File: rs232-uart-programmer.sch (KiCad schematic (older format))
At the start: 45 parts, among them J1 DB9_Female_MountingHoles, J2 Barrel_Jack, J3 Conn_01x03_Male, J4 Conn_01x02_Male, J5 USB_B, J6 Conn_01x05_Male, Q1 2N3905, Q2 AO3407A, Q3 2N3905, U1 L7805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

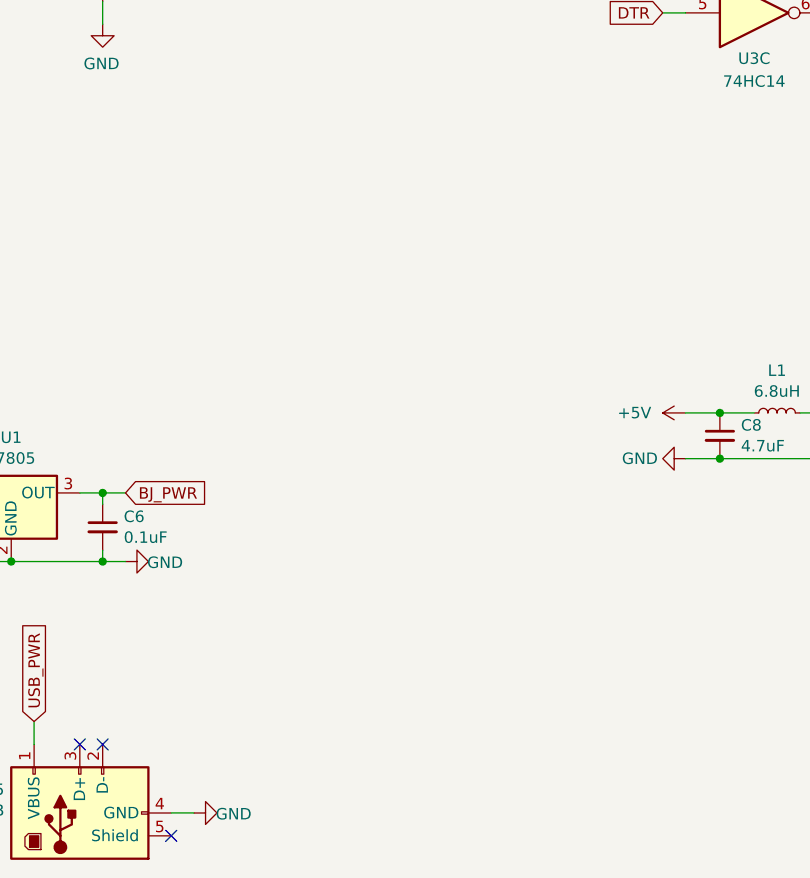
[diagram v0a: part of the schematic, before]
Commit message: Added mounting holes
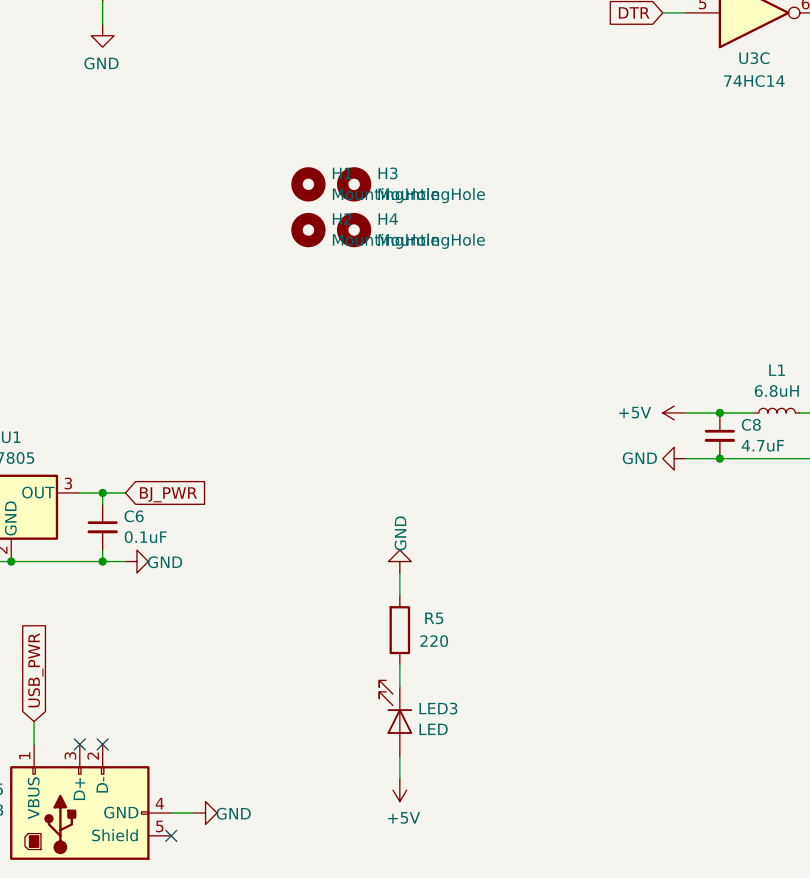
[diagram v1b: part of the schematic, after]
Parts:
- added H1, H2, H3, H4: MountingHole, MountingHole:MountingHole_3mm, symbol Mechanical:MountingHole
- added LED3: LED, LED_THT:LED_D5.0mm, symbol Device:LED
- added R5: 220, Resistor_THT:R_Axial_DIN0207_L6.3mm_D2.5mm_P10.16mm_Horizontal, symbol Device:R
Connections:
- net +5V: now also LED3.2 (A)
- net GND: now also R5.2
- new net: LED3.1 (K), R5.1
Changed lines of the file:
@@
 	7950 1850 8000 1850
 $Comp
-L power:+5V #PWR?
+L power:+5V #PWR032
 U 1 1 613E50BD
 P 7550 1600
-F 0 "#PWR?" H 7550 1450 50  0001 C CNN
+F 0 "#PWR032" H 7550 1450 50  0001 C CNN
 F 1 "+5V" V 7550 1800 50  0000 C CNN
 F 2 "" H 7550 1600 50  0001 C CNN
@@
 Wire Wire Line
 	7550 1600 7600 1600
+$Comp
+L Device:LED LED3
+U 1 1 613E63BE
+P 5650 6700
+F 0 "LED3" V 5595 6779 50  0000 L CNN
+F 1 "LED" V 5686 6779 50  0000 L CNN
+F 2 "LED_THT:LED_D5.0mm" H 5650 6700 50  0001 C CNN
+F 3 "~" H 5650 6700 50  0001 C CNN
+	1    5650 6700
+	0    1    1    0
+$EndComp
+$Comp
+L power:+5V #PWR031
+U 1 1 613E65F0
+P 5650 6950
+F 0 "#PWR031" H 5650 6800 50  0001 C CNN
+F 1 "+5V" H 5665 7123 50  0000 C CNN
+F 2 "" H 5650 6950 50  0001 C CNN
+F 3 "" H 5650 6950 50  0001 C CNN
+	1    5650 6950
+	1    0    0    1
+$EndComp
+$Comp
+L power:GND #PWR030
+U 1 1 613E6704
+P 5650 6050
+F 0 "#PWR030" H 5650 5800 50  0001 C CNN
+F 1 "GND" V 5655 5877 50  0000 C CNN
+F 2 "" H 5650 6050 50  0001 C CNN
+F 3 "" H 5650 6050 50  0001 C CNN
+	1    5650 6050
+	1    0    0    1
+$EndComp
+$Comp
+L Device:R R5
+U 1 1 613E6813
+P 5650 6300
+F 0 "R5" H 5800 6250 50  0000 C CNN
+F 1 "220" H 5800 6350 50  0000 C CNN
+F 2 "Resistor_THT:R_Axial_DIN0207_L6.3mm_D2.5mm_P10.16mm_Horizontal" V 5580 6300 50  0001 C CNN
+F 3 "~" H 5650 6300 50  0001 C CNN
+	1    5650 6300
+	1    0    0    1
+$EndComp
+Wire Wire Line
+	5650 6050 5650 6150
+Wire Wire Line
+	5650 6450 5650 6550
+Wire Wire Line
+	5650 6850 5650 6950
+$Comp
+L Mechanical:MountingHole H3
+U 1 1 6140AC7E
+P 5450 4350
+F 0 "H3" H 5550 4396 50  0000 L CNN
+F 1 "MountingHole" H 5550 4305 50  0000 L CNN
+F 2 "MountingHole:MountingHole_3mm" H 5450 4350 50  0001 C CNN
+F 3 "~" H 5450 4350 50  0001 C CNN
+	1    5450 4350
+	1    0    0    -1
+$EndComp
+$Comp
+L Mechanical:MountingHole H4
+U 1 1 6140ADDA
+P 5450 4550
+F 0 "H4" H 5550 4596 50  0000 L CNN
+F 1 "MountingHole" H 5550 4505 50  0000 L CNN
+F 2 "MountingHole:MountingHole_3mm" H 5450 4550 50  0001 C CNN
+F 3 "~" H 5450 4550 50  0001 C CNN
+	1    5450 4550
+	1    0    0    -1
+$EndComp
+$Comp
+L Mechanical:MountingHole H2
+U 1 1 6140AE60
+P 5250 4550
+F 0 "H2" H 5350 4596 50  0000 L CNN
+F 1 "MountingHole" H 5350 4505 50  0000 L CNN
+F 2 "MountingHole:MountingHole_3mm" H 5250 4550 50  0001 C CNN
+F 3 "~" H 5250 4550 50  0001 C CNN
+	1    5250 4550
+	1    0    0    -1
+$EndComp
+$Comp
+L Mechanical:MountingHole H1
+U 1 1 6140AEEC
+P 5250 4350
+F 0 "H1" H 5350 4396 50  0000 L CNN
+F 1 "MountingHole" H 5350 4305 50  0000 L CNN
+F 2 "MountingHole:MountingHole_3mm" H 5250 4350 50  0001 C CNN
+F 3 "~" H 5250 4350 50  0001 C CNN
+	1    5250 4350
+	1    0    0    -1
+$EndComp
 $EndSCHEMATC
